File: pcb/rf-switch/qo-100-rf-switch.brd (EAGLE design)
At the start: 66 x 40 mm, 40 parts, among them CON1 4P-SH-SIDE, U1 F2915NBGK, U2 ADP7142AUJZ-3.3, U3 MCP23008

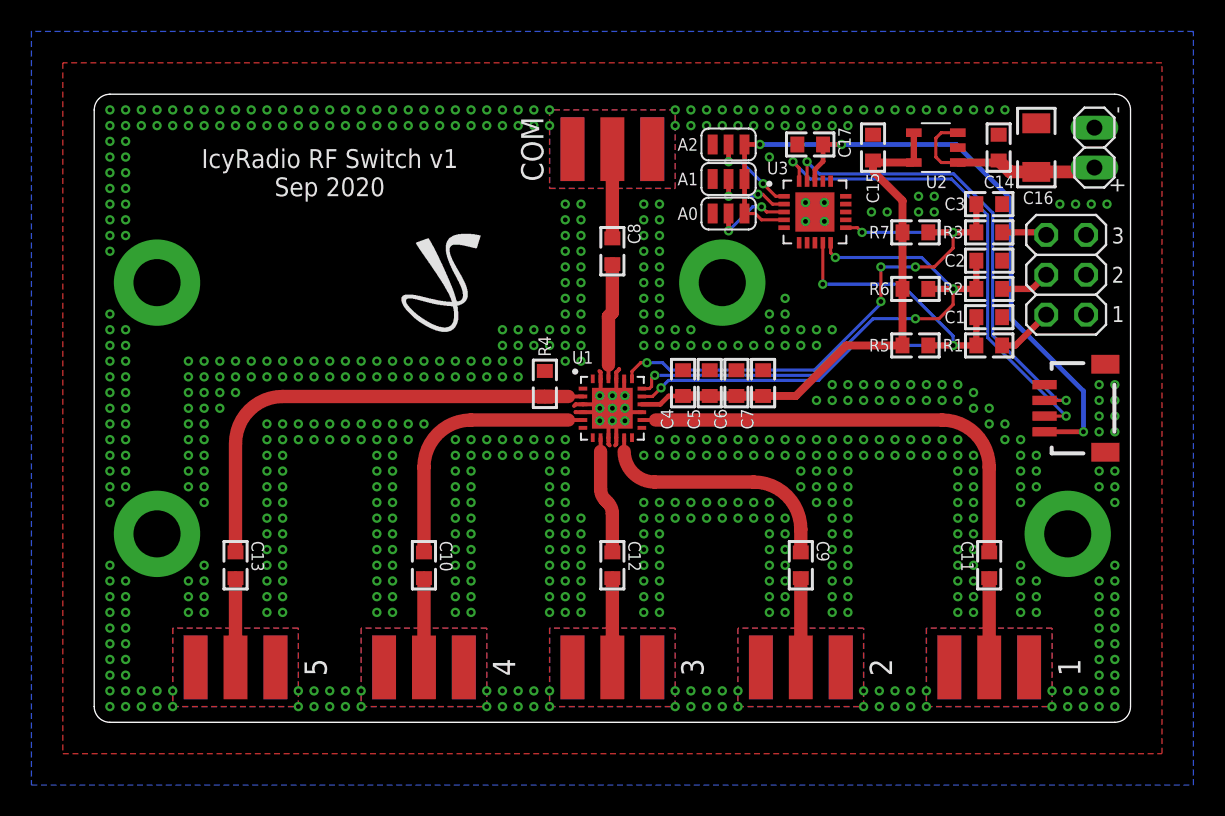
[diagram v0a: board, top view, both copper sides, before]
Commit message: RF Switch v2: Allow chosing interface or standalone power in software
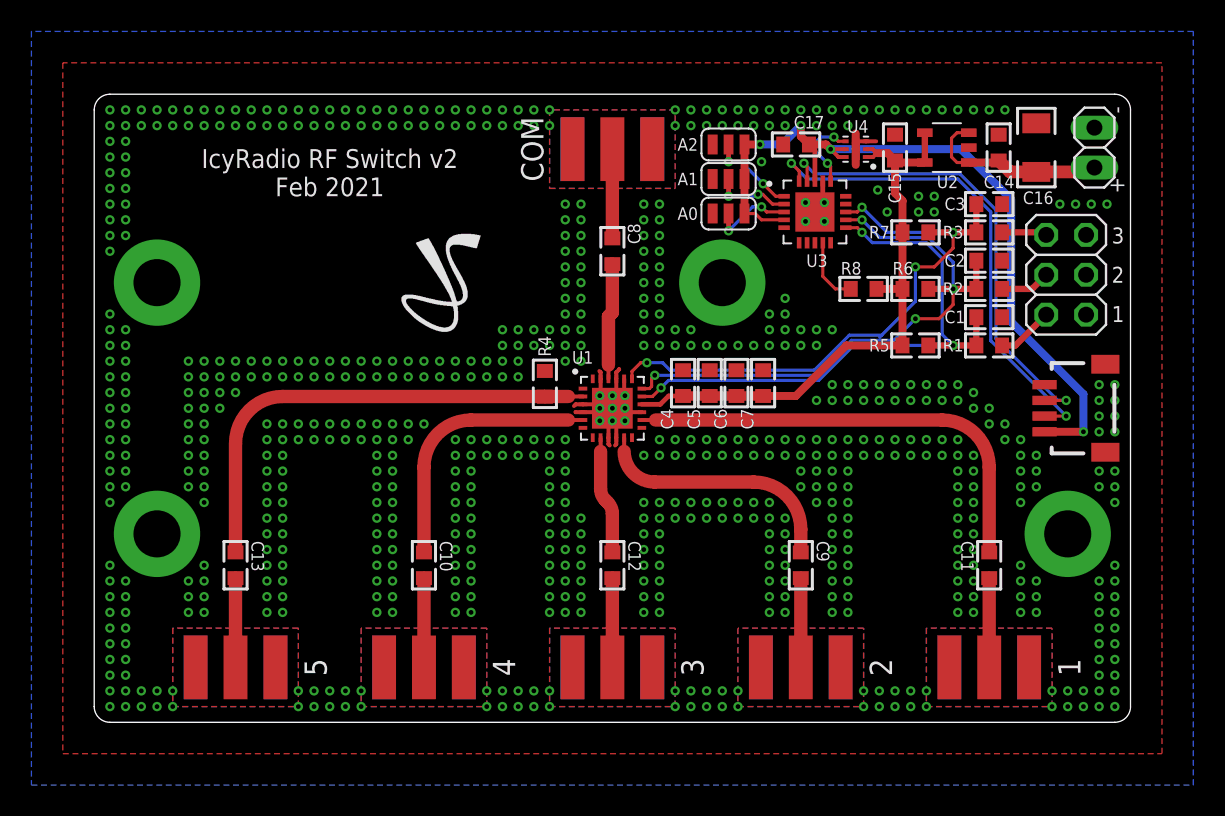
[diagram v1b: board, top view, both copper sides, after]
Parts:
- added R8: 100K Ohms, Resistor:RES0603
- added U4: MIC94305, Microchip:DFN6
- C17: value 1uF -> 10uF
- R5, R6, R7: value 1K Ohms -> 10K Ohms
- moved C15 1.40 mm to (51.0, 36.6)
- moved C17 0.90 mm to (44.7, 36.8)
- moved U2 0.70 mm to (54.3, 36.6)
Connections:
- new net PWR_FILTER_EN: U3.16, U4.4
- new net PWR_SENSE: R8.1, U3.9
- net 3V3: now also R8.2, U4.1, U4.2
- net 3V3_IO: now also U4.5, U4.6
- net GND: now also U4.3, U4.7
- net SW_V1: now also U3.11; no longer U3.9
- net SW_V2: now also U3.12; no longer U3.10
- net SW_V3: now also U3.13; no longer U3.11
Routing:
- net GND: track 13.5 -> 19.0 mm, vias 699 -> 698
- net PWR_FILTER_EN: track 0.00 -> 5.07 mm, vias 0 -> 2
- net PWR_SENSE: track 0.00 -> 4.25 mm
- net 3V3: track 35.3 -> 38.6 mm
- net 3V3_IO: track 48.4 -> 50.7 mm, vias 3 -> 4
- net N$16: track 13.5 -> 12.2 mm
- net SW_V3: track 38.8 -> 39.5 mm, vias 6 -> 4
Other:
- board text added: "IcyRadio RF Switch v2 Feb 2021"
- board text removed: "IcyRadio RF Switch v1 Sep 2020"
